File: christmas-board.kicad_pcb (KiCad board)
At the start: 2 copper layers, 96.4 x 97.9 mm, 47 parts, among them J1 Conn_01x02_Female, Q1 Q_NPN_BCE, Q2 Q_NPN_BCE, Q3 Q_NPN_BCE, Q4 Q_NPN_BCE, Q5 Q_NPN_BCE, SW1 SW_Push, SW2 SW_Push, U1 595_SHIFT, U2 555

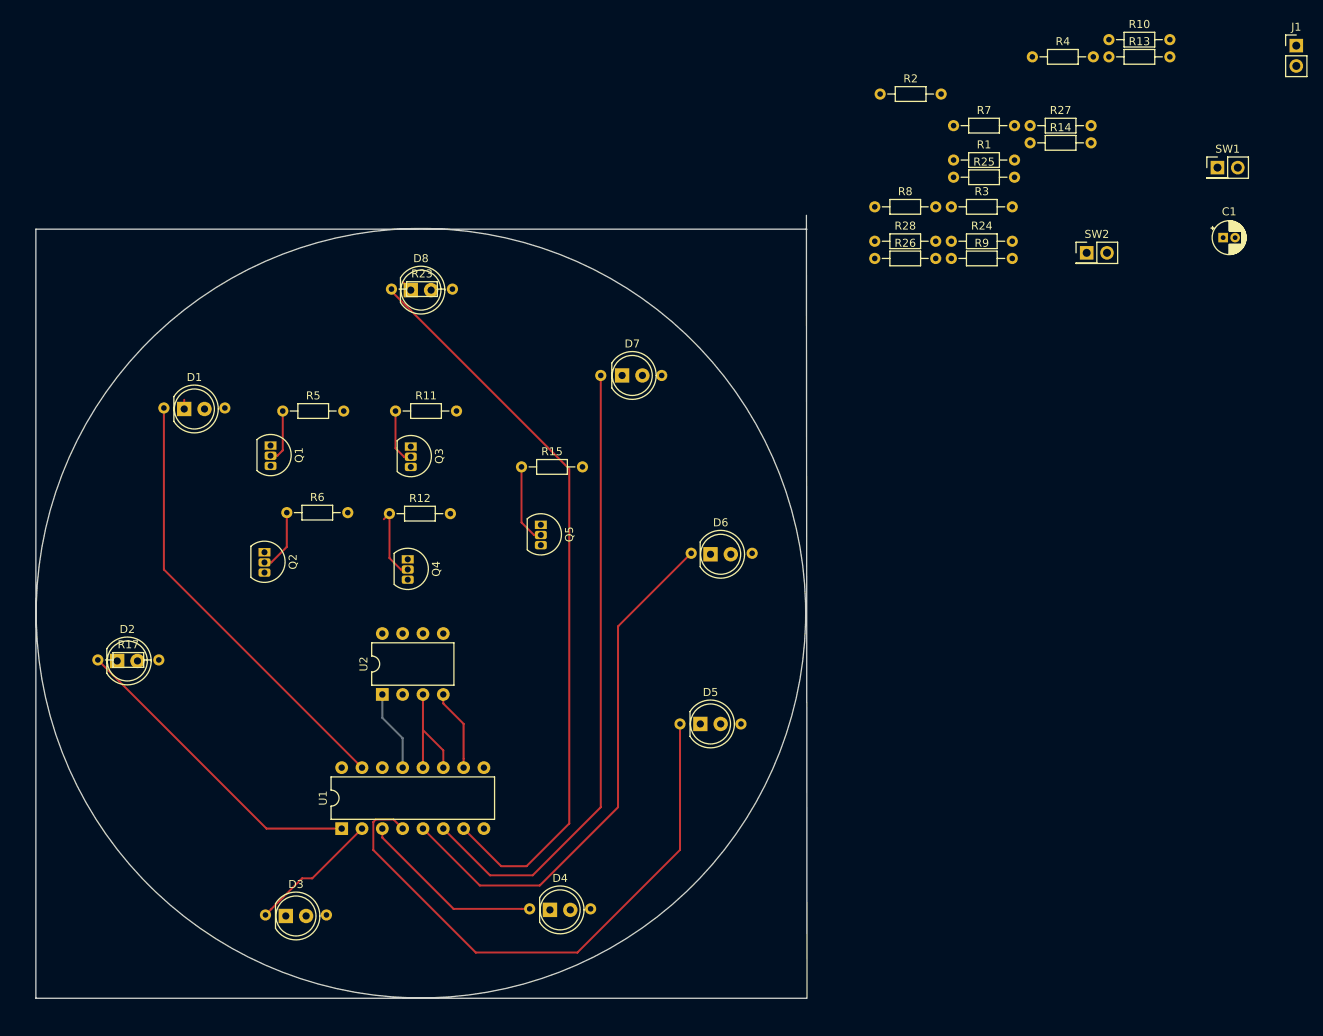
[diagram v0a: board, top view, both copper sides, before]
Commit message: LED routing complete
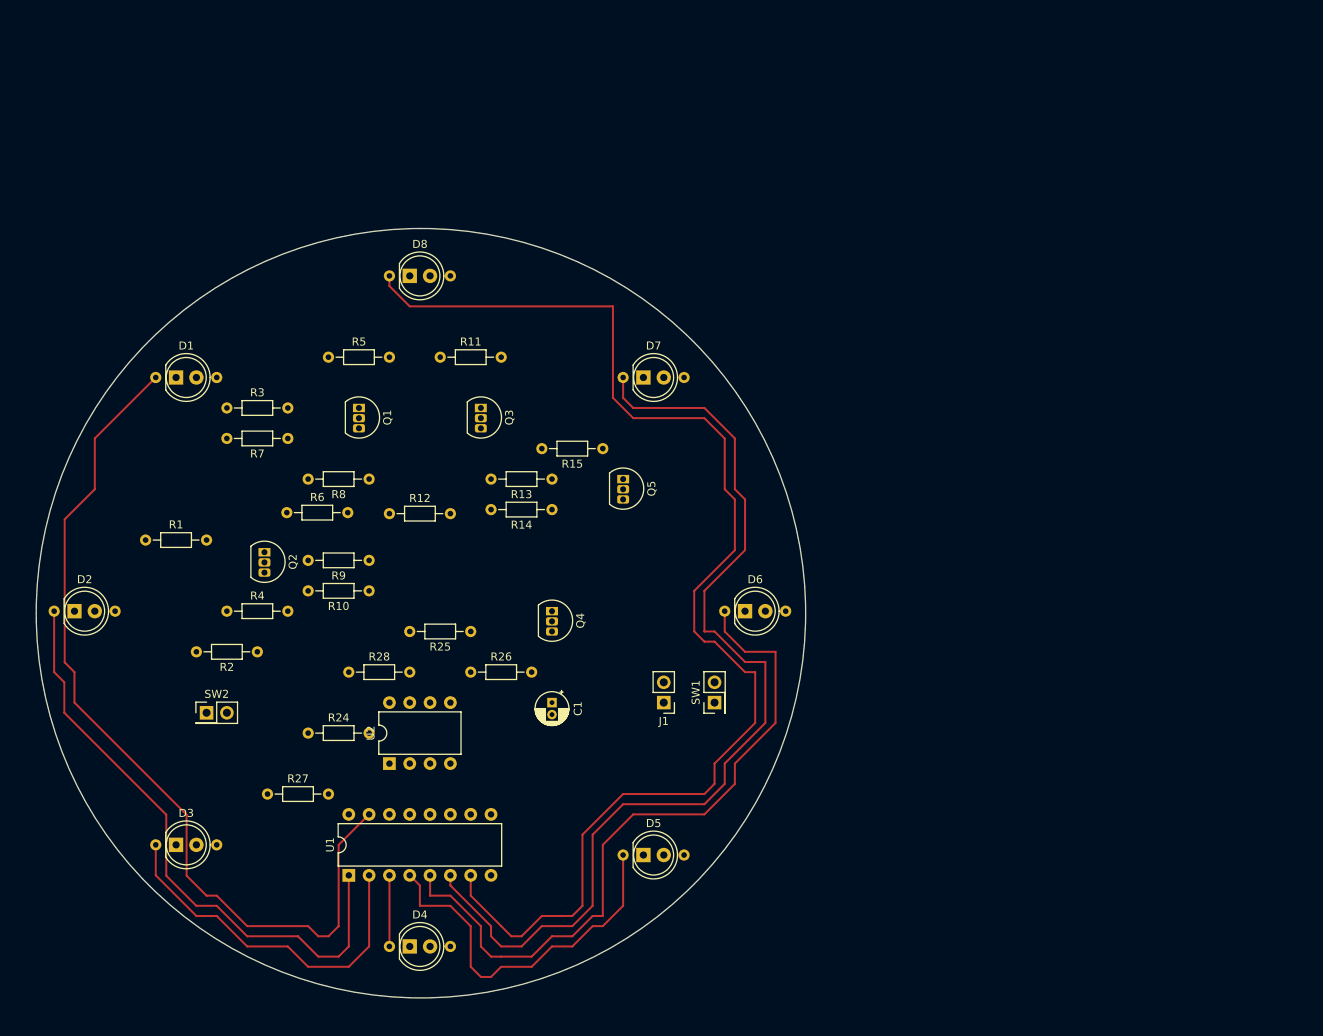
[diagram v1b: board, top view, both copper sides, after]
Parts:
- Q1, Q2, Q3, Q4, Q5: value Q_NPN_BCE -> Q_NPN_CBE
- R17, R23: moved to B.Cu
- moved R27 126.8 mm to (91.4, 111.8)
- moved SW2 124.1 mm to (83.8, 101.6)
- moved R4 122.2 mm to (86.4, 88.9)
- moved R10 115.3 mm to (104.1, 86.4), turned to 180 degrees
- moved J1 114.0 mm to (141.0, 100.3), turned to 180 degrees
- moved R1 111.6 mm to (76.2, 80.0)
- moved R2 104.5 mm to (90.2, 94.0), turned to 180 degrees
- moved C1 102.1 mm to (127.0, 100.3), turned to 270 degrees
- moved R24 101.2 mm to (96.5, 104.1)
- moved R3 94.0 mm to (86.4, 63.5)
- moved R7 91.9 mm to (94.0, 67.3), turned to 180 degrees
- moved SW1 91.8 mm to (147.3, 100.3), turned to 90 degrees
- moved R13 87.4 mm to (127.0, 72.4), turned to 180 degrees
- moved R28 85.0 mm to (101.6, 96.5)
- moved R25 82.9 mm to (116.8, 91.4), turned to 180 degrees
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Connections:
- Q5 pad 1: Net-(Q5-Pad1) -> /PULL_HIGH
- Q5 pad 2: /PULL_HIGH -> Net-(Q5-Pad2)
- R10 pad 1: Net-(Q4-Pad1) -> Net-(Q4-Pad2)
- R11 pad 1: Net-(Q3-Pad2) -> Net-(Q3-Pad1)
- R12 pad 1: Net-(Q4-Pad2) -> Net-(Q4-Pad1)
- R13 pad 1: Net-(Q5-Pad1) -> Net-(Q5-Pad2)
- R13 pad 2: Net-(Q3-Pad2) -> Net-(Q3-Pad1)
- R14 pad 1: Net-(Q5-Pad1) -> Net-(Q5-Pad2)
- R14 pad 2: Net-(Q4-Pad2) -> Net-(Q4-Pad1)
- R3 pad 1: Net-(Q1-Pad1) -> Net-(Q1-Pad2)
- R4 pad 1: Net-(Q2-Pad1) -> Net-(Q2-Pad2)
- R5 pad 1: Net-(Q1-Pad2) -> Net-(Q1-Pad1)
- R6 pad 1: Net-(Q2-Pad2) -> Net-(Q2-Pad1)
- R7 pad 1: Net-(Q3-Pad1) -> Net-(Q3-Pad2)
- R7 pad 2: Net-(Q1-Pad2) -> Net-(Q1-Pad1)
- R8 pad 1: Net-(Q3-Pad1) -> Net-(Q3-Pad2)
- R8 pad 2: Net-(Q2-Pad2) -> Net-(Q2-Pad1)
- R9 pad 1: Net-(Q4-Pad1) -> Net-(Q4-Pad2)
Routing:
- net /LED_H: track 93.3 -> 158.5 mm
- net /LED_A: track 55.2 -> 111.5 mm
- net /LED_G: track 79.6 -> 125.0 mm
- net /LED_B: track 39.2 -> 75.3 mm
- net /LED_C: track 16.5 -> 45.2 mm
- net /LED_E: track 72.5 -> 46.4 mm
- net /LED_F: track 66.9 -> 88.0 mm
- net /555_OUT: track 14.9 -> 0.00 mm
- net /LED_D: track 23.2 -> 8.89 mm
- net GND: track 12.8 -> 0.00 mm
- net VCC: track 10.2 -> 0.00 mm
- net /PULL_HIGH: track 10.0 -> 0.00 mm
- net Net-(Q4-Pad2): track 9.42 -> 0.00 mm
- net Net-(Q2-Pad2): track 7.88 -> 0.00 mm
- net Net-(Q3-Pad2): track 7.00 -> 0.00 mm
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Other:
- board size 96.4 x 97.9 mm -> 96.2 x 96.2 mm

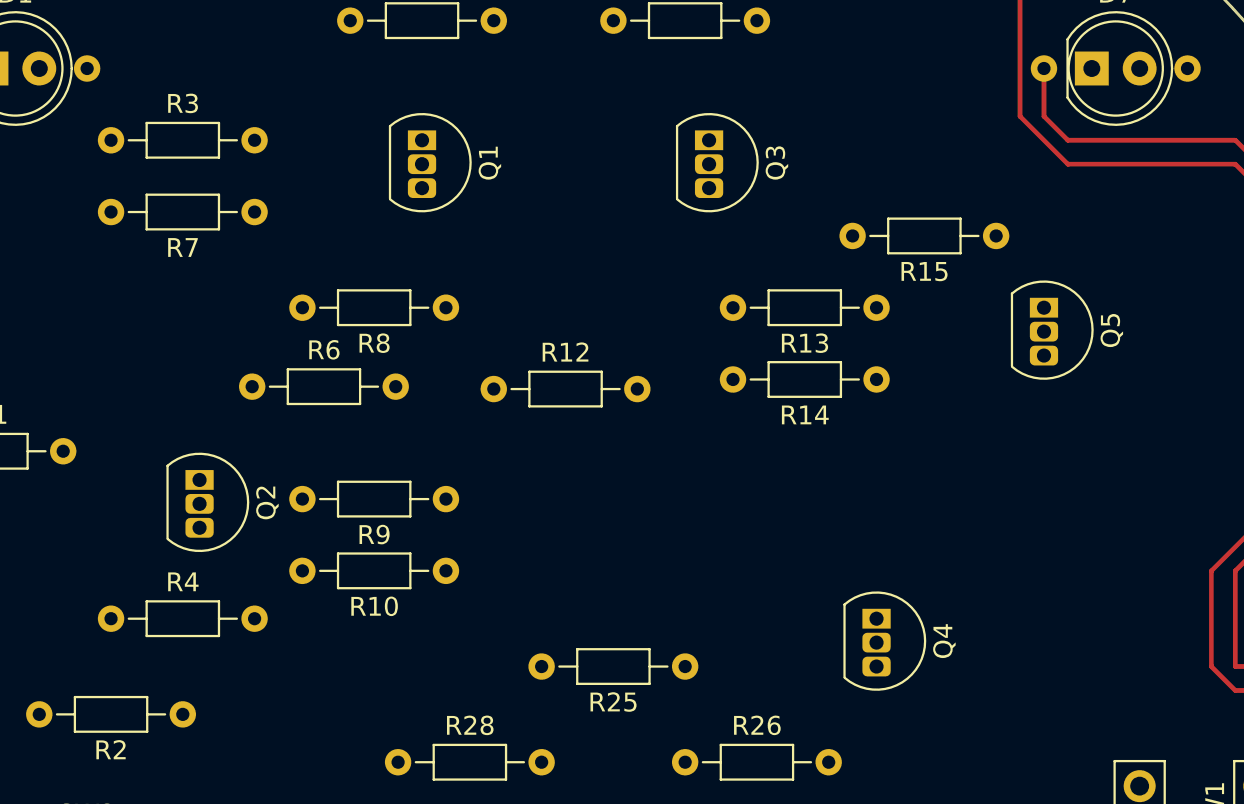
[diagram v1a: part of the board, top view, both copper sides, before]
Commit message: fix footprint on npn - swich to EBC ro CBE
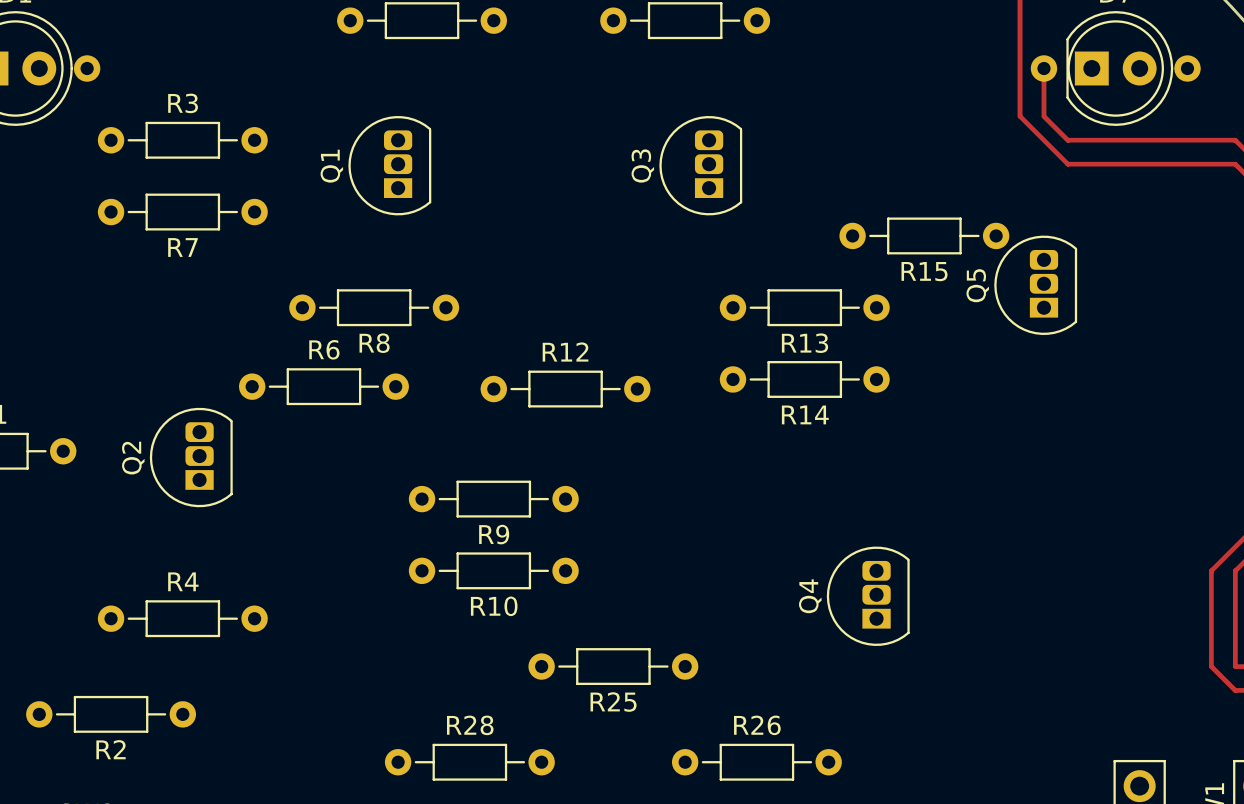
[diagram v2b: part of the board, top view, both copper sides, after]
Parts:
- Q1, Q2, Q3, Q4, Q5: value Q_NPN_CBE -> Q_NPN_EBC
- moved R10 6.35 mm to (110.5, 86.4)
- moved R9 6.35 mm to (110.5, 82.5)
- moved Q1 2.84 mm to (101.6, 66.0), turned to 90 degrees
- moved Q3 2.54 mm to (118.1, 66.0), turned to 90 degrees
- turned Q2 to 90 degrees
- turned Q4 to 90 degrees
- turned Q5 to 90 degrees
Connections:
- Q1 pad 1: Net-(Q1-Pad1) -> GND
- Q1 pad 3: GND -> Net-(Q1-Pad3)
- Q2 pad 1: Net-(Q2-Pad1) -> GND
- Q2 pad 3: GND -> Net-(Q2-Pad3)
- Q3 pad 1: Net-(Q3-Pad1) -> GND
- Q3 pad 3: GND -> Net-(Q3-Pad3)
- Q4 pad 1: Net-(Q4-Pad1) -> GND
- Q4 pad 3: GND -> Net-(Q4-Pad3)
- Q5 pad 1: /PULL_HIGH -> GND
- Q5 pad 3: GND -> /PULL_HIGH
- R11 pad 1: Net-(Q3-Pad1) -> Net-(Q3-Pad3)
- R12 pad 1: Net-(Q4-Pad1) -> Net-(Q4-Pad3)
- R13 pad 2: Net-(Q3-Pad1) -> Net-(Q3-Pad3)
- R14 pad 2: Net-(Q4-Pad1) -> Net-(Q4-Pad3)
- R5 pad 1: Net-(Q1-Pad1) -> Net-(Q1-Pad3)
- R6 pad 1: Net-(Q2-Pad1) -> Net-(Q2-Pad3)
- R7 pad 2: Net-(Q1-Pad1) -> Net-(Q1-Pad3)
- R8 pad 2: Net-(Q2-Pad1) -> Net-(Q2-Pad3)

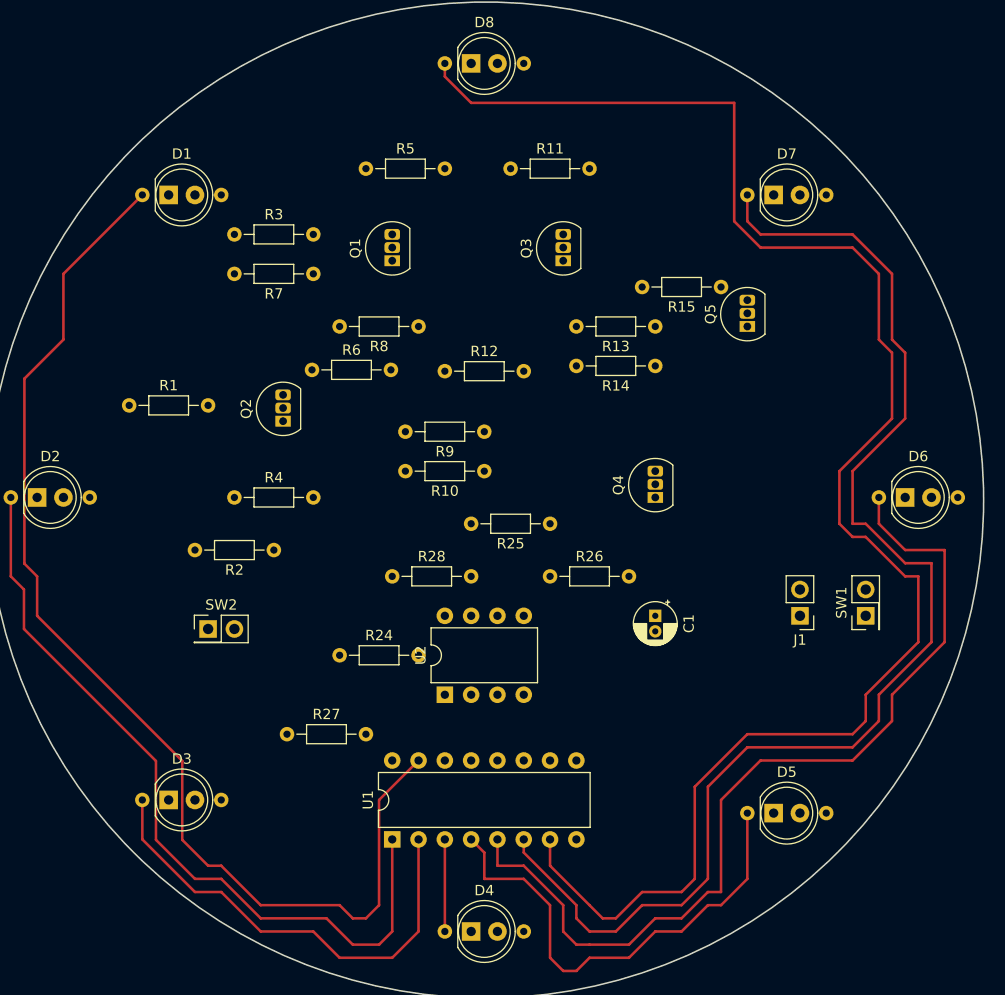
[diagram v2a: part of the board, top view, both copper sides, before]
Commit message: signal tracks complete
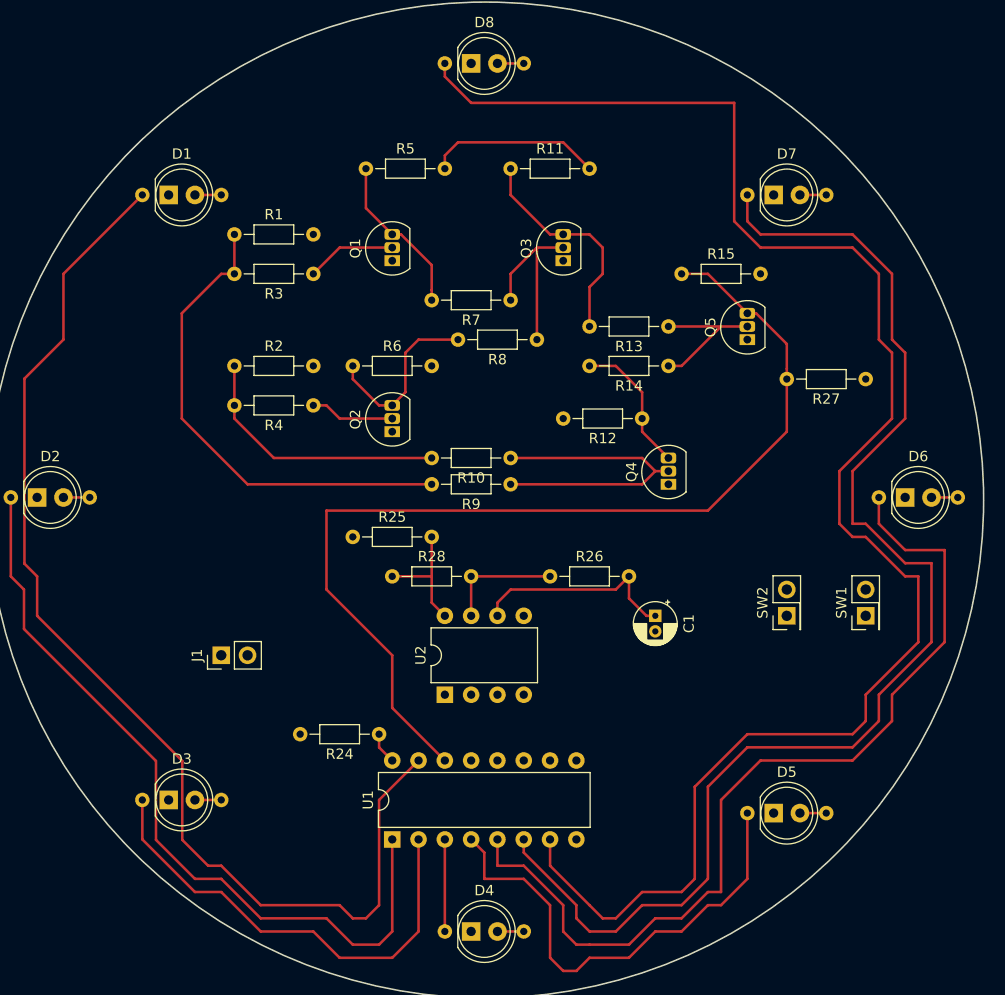
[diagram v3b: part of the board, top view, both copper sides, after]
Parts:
- moved R27 65.6 mm to (147.3, 77.5), turned to 180 degrees
- moved J1 56.0 mm to (85.1, 104.1), turned to 90 degrees
- moved SW2 55.9 mm to (139.7, 100.3), turned to 90 degrees
- moved R12 19.6 mm to (125.7, 81.3), turned to 180 degrees
- moved R1 19.4 mm to (86.4, 63.5)
- moved R7 19.2 mm to (113.0, 69.8)
- moved R25 19.1 mm to (97.8, 92.7), turned to 0 degrees
- moved R2 18.2 mm to (86.4, 76.2), turned to 0 degrees
- moved R4 11.7 mm to (94.0, 80.0), turned to 180 degrees
- moved R8 11.5 mm to (115.6, 73.7)
- moved Q2 10.6 mm to (101.6, 82.5)
- moved R24 8.52 mm to (100.3, 111.8), turned to 180 degrees
- moved R3 8.52 mm to (94.0, 67.3), turned to 180 degrees
- moved R9 5.68 mm to (113.0, 87.6)
- moved R15 4.02 mm to (129.5, 67.3), turned to 0 degrees
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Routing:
- net /PULL_HIGH: track 0.00 -> 97.9 mm
- net /XOR_IN_A: track 0.00 -> 47.4 mm
- net Net-(Q4-Pad2): track 0.00 -> 30.3 mm
- net /LED_E: track 46.4 -> 72.1 mm
- net Net-(Q3-Pad3): track 0.00 -> 21.7 mm
- net Net-(C1-Pad1): track 0.00 -> 20.4 mm
- net Net-(Q3-Pad2): track 0.00 -> 17.6 mm
- net Net-(Q2-Pad3): track 0.00 -> 17.3 mm
- net VCC: track 0.00 -> 16.8 mm
- net Net-(Q1-Pad3): track 0.00 -> 15.8 mm
- net Net-(Q5-Pad2): track 0.00 -> 14.3 mm
- net Net-(Q4-Pad3): track 0.00 -> 13.5 mm
- net Net-(R25-Pad2): track 0.00 -> 12.0 mm
- net Net-(R26-Pad1): track 0.00 -> 11.4 mm
- net Net-(Q1-Pad2): track 0.00 -> 8.67 mm
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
